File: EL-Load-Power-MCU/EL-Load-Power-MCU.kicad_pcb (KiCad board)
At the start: 4 copper layers, 175 x 72.5 mm, 115 parts, among them J1 Conn_01x02, J10 Power for serial interface, J11 Conn_02x08_Odd_Even, J12 Conn_01x05_Pin, J2 Screw_Terminal_01x02, J3 Touchscreen, J4 JST-S6B-PH-SM4, J5 PN sensor, J6 PN sensor, J7 Conn_02x08_Odd_Even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

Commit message: Fixed Panel 1r1 and Power-MCU 2r2 versions
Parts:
- C6: value 1u -> 10u
- U11: value 24LC64 -> 24C64

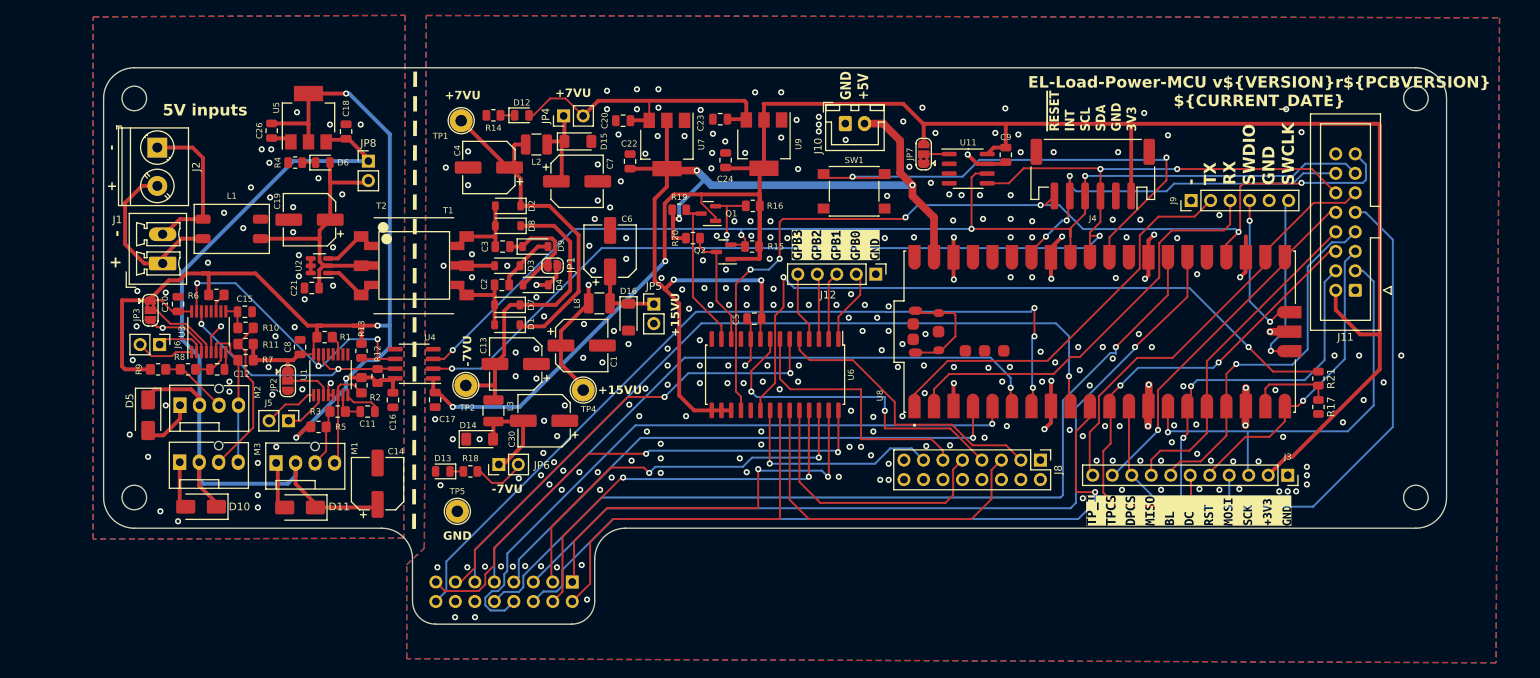
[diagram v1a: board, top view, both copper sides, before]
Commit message: Fixes to Power-MCU board.
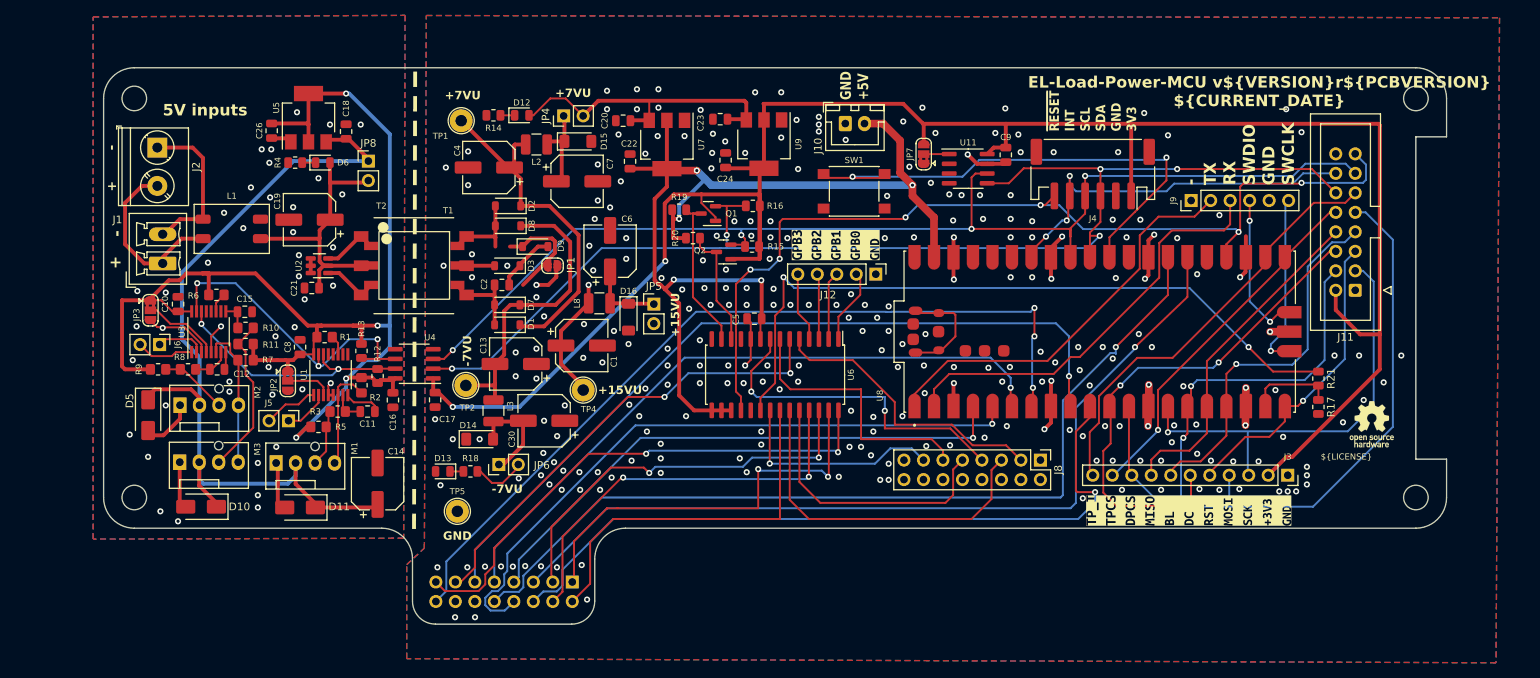
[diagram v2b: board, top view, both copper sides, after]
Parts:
- removed C3: 1u, Capacitor_SMD:C_0805_2012Metric
- removed D4: MBR0530, Diode_SMD:D_SOD-123
- added PCB1: Logo_Open_Hardware_Small, Symbol:OSHW-Logo_5.7x6mm_SilkScreen, F.Cu at (179.7, 72.0)
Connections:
- C13 pad 2: Net-(D7-K) -> Net-(D7-A)
- C21 pad 1: GND_ISO -> Net-(U2-CLK)
- D7 pad 1: Net-(D7-K) -> Net-(D1-A)
- D7 pad 2: Net-(D1-A) -> Net-(D7-A)
- D8 pad 1: Net-(D7-K) -> Net-(D2-A)
- D8 pad 2: Net-(D2-A) -> Net-(D7-A)
- L3 pad 2: Net-(D7-K) -> Net-(D7-A)
- TP2 pad 1: Net-(D7-K) -> Net-(D7-A)
- U2 pad 5: GND_ISO -> +5V_ISO
- U2 pad 6: GND_ISO -> Net-(U2-CLK)
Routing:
- net Net-(D7-K): track 39.4 -> 0.00 mm
- net (no net): track 0.00 -> 39.4 mm
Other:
- outline, holes or cut-outs redrawn
- board text added: "${LICENSE}"

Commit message: Did #7, #10 and few items from #2
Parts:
- added C25: 100u, Capacitor_SMD:CP_Elec_8x10.5, F.Cu at (11.9, 36.3)
- added C27: 200n, Capacitor_SMD:C_0805_2012Metric, F.Cu at (29.3, 35.0)
- added C28: 100u, Capacitor_SMD:CP_Elec_8x10.5, F.Cu at (35.1, 32.8)
- added D17: 1N5819WS, Diode_SMD:D_SMA, F.Cu at (21.4, 42.8)
- added D18: BZV55B5V6, Diode_SMD:D_MiniMELF, F.Cu at (35.0, 46.5)
- added F1: 1A, Fuse:Fuse_1206_3216Metric, F.Cu at (16.2, 42.8)
- added JP10: Select 5V source, Connector_PinHeader_2.54mm:PinHeader_1x03_P2.54mm_Vertical, F.Cu at (50.3, 40.3)
- added JP9: Jumper_2_Bridged, Connector_PinHeader_2.54mm:PinHeader_1x02_P2.54mm_Vertical, F.Cu at (11.8, 42.7)
- added L4: 100u / 300mA, Inductor_SMD:L_Bourns_SRN6045TA, F.Cu at (26.7, 42.8)
- added R22: 0.3, Resistor_SMD:R_0805_2012Metric_Pad1.20x1.40mm_HandSolder, F.Cu at (19.4, 36.7)
- added R23: 10k, Resistor_SMD:R_0805_2012Metric, F.Cu at (25.9, 32.2)
- added R24: 3k3, Resistor_SMD:R_0805_2012Metric, F.Cu at (23.0, 31.4)
- added U10: MC34063AD, Package_SO:SOIC-8_3.9x4.9mm_P1.27mm, F.Cu at (24.3, 36.1)
- J2: value Screw_Terminal_01x02 -> Conn_01x02; footprint TerminalBlock_Phoenix:TerminalBlock_Phoenix_PT-1,5-2-5.0-H_1x02_P5.00mm_Horizontal -> Connector_Phoenix_MC:PhoenixContact_MCV_1,5_2-G-3.81_1x02_P3.81mm_Vertical
- JP8: value Jumper_2_Bridged -> Select Fan Voltage; footprint Connector_PinHeader_2.54mm:PinHeader_1x02_P2.54mm_Vertical -> Connector_PinHeader_2.54mm:PinHeader_1x03_P2.54mm_Vertical
- moved J1 25.3 mm to (12.1, 74.2)
- moved L1 24.3 mm to (12.1, 61.6), turned to 90 degrees
- moved JP8 23.0 mm to (29.5, 49.9), turned to -90 degrees
- moved J2 19.4 mm to (12.1, 52.9), turned to 90 degrees
- moved C26 5.74 mm to (42.0, 32.5)
- moved C18 5.74 mm to (51.7, 32.6)
- moved U5 5.74 mm to (46.8, 30.8)
- moved R4 5.65 mm to (45.1, 37.1)
- moved D6 5.63 mm to (48.7, 37.3)
- moved C19 0.62 mm to (41.5, 45.9)
- turned D7 to 0 degrees
- turned D8 to 0 degrees
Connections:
- C14 pad 1: +5V_FANS -> +V_FANS
- C18 pad 2: +5V_FANS -> +V_FANS
- D10 pad 1: +5V_FANS -> +V_FANS
- D11 pad 1: +5V_FANS -> +V_FANS
- D5 pad 1: +5V_FANS -> +V_FANS
- J2 pad 1: Net-(J1-Pin_2) -> +12V_ISO
- J2 pad 2: Net-(J1-Pin_1) -> GND_ISO
- J7 pad 14: GND -> +3V3
- JP8 pad 1: +5V_FANS -> +5V_ISO
- JP8 pad 2: +5V_ISO -> +V_FANS
- L1 pad 4: +5V_ISO -> Net-(JP10-A)
- M1 pad 2: +5V_FANS -> +V_FANS
- M2 pad 2: +5V_FANS -> +V_FANS
- M3 pad 2: +5V_FANS -> +V_FANS
- U5 pad 3: +5V_FANS -> +V_FANS
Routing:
- net +5V_FANS: track 110.4 -> 0.00 mm
- net +V_FANS: track 0.00 -> 109.2 mm, vias 0 -> 1
- net Net-(JP10-A): track 0.00 -> 57.8 mm, vias 0 -> 1
- net (no net): track 39.4 -> 0.00 mm
- net /Standalone Power/5Vout: track 0.00 -> 38.4 mm
- net Net-(D7-A): track 0.00 -> 38.1 mm
- net +3V3: track 263.7 -> 298.0 mm
- net +12V_ISO: track 0.00 -> 28.0 mm
- net Net-(J1-Pin_2): track 20.6 -> 5.57 mm
- net Net-(U10-Vin): track 0.00 -> 13.9 mm
- net Net-(D17-K): track 0.00 -> 11.7 mm
- net Net-(J1-Pin_1): track 23.5 -> 13.3 mm
- net Net-(U10-DC): track 0.00 -> 8.77 mm
- net +5V_ISO: track 37.0 -> 43.8 mm
- net Net-(D9-K): track 13.9 -> 8.38 mm
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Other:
- board size 175 x 72.5 mm -> 185 x 72.5 mm
- board text added: "12V Fan 5V"
- board text added: "12V in"
- board text added: "12V->5V enable"
- board text added: "5V Direct"
- board text added: "5V in"
- board text added: "From 12V"
- board text removed: "5V inputs"

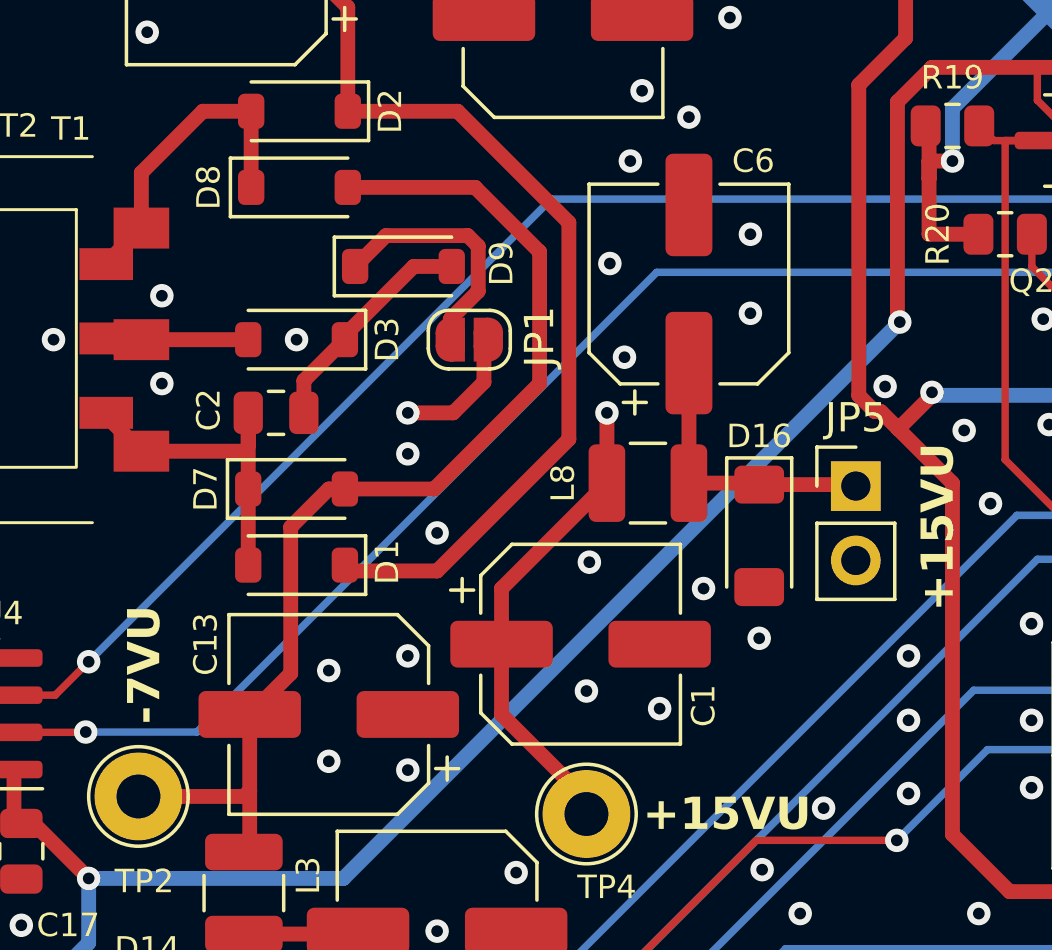
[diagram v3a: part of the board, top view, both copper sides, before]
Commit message: Added +15VU led, fixed JP1
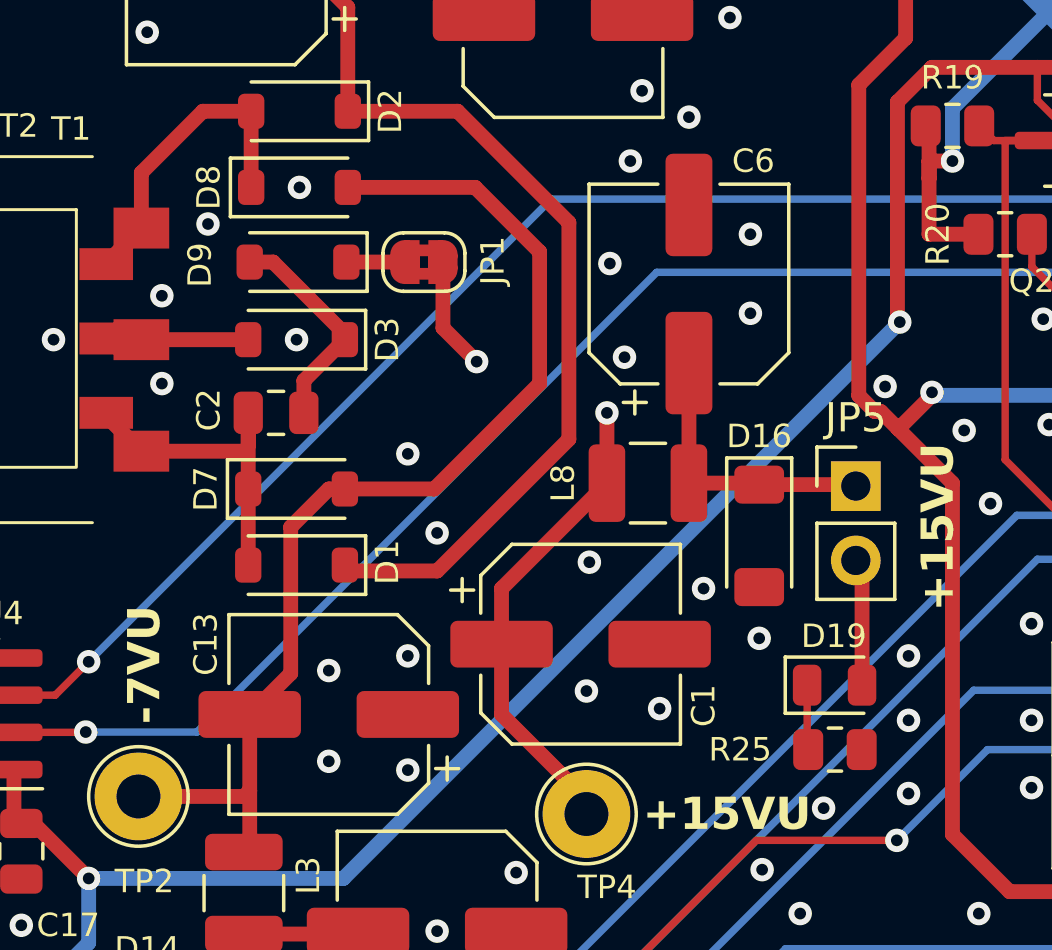
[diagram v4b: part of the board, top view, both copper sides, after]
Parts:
- added D19: LED, LED_SMD:LED_0805_2012Metric, F.Cu at (85.5, 63.1)
- added R25: 20k, Resistor_SMD:R_0805_2012Metric, F.Cu at (85.5, 65.3)
- JP1: value SolderJumper_2_Open -> SolderJumper_2_Bridged; footprint Jumper:SolderJumper-2_P1.3mm_Open_RoundedPad1.0x1.5mm -> Jumper:SolderJumper-2_P1.3mm_Bridged2Bar_RoundedPad1.0x1.5mm
- moved D9 3.60 mm to (67.1, 48.7), turned to 180 degrees
- moved JP1 3.07 mm to (71.4, 48.7)
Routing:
- net Net-(D9-K): track 8.38 -> 2.00 mm
- net +15VU: track 64.6 -> 69.0 mm
- net Net-(JP1-B): track 27.7 -> 25.4 mm
- net Net-(D19-K): track 0.00 -> 2.22 mm
- net GND: vias 269 -> 271
